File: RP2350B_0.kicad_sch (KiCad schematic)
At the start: 29 parts, among them CN4 W25Q128FVIQ_Connector, J6 Conn_01x02, X3 12MHz

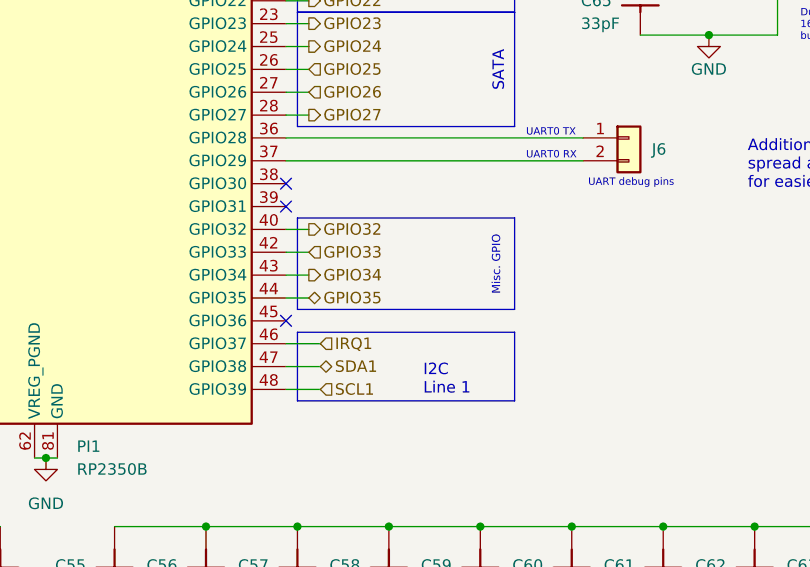
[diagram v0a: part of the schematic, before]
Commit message: Switched USB7206C IC to USB7205C
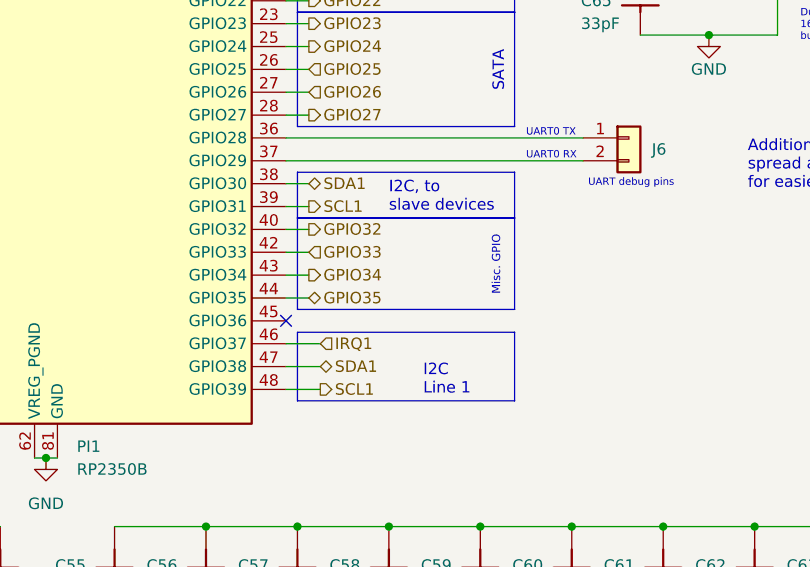
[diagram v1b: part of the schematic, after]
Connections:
- net SCL1: now also PI1.39 (GPIO31)
- net SDA1: now also PI1.38 (GPIO30)
- no-connect marks 8 -> 6
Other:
- note added: "I2C, to slave devices"
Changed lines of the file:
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@@
+		)
+	)
+	(rectangle
+		(start 129.54 111.76)
+		(end 153.67 116.84)
+		(stroke
+			(width 0)
+			(type default)
+		)
+		(fill
+			(type none)
 		)
 	)
@@
 		)
 	)
+	(text "I2C, to\nslave devices"
+		(exclude_from_sim no)
+		(at 139.7 114.554 0)
+		(effects
+			(font
+				(size 1.27 1.27)
+			)
+			(justify left)
+		)
+	)
 	(text "Dual 33pF capacitors is to achieve\n16.5pF + ~3pF (parasitic) = ~19.5pF total,\nbut 220ohm res is eyeballed, needs testing"
 		(exclude_from_sim no)
@@
 	)
 	(no_connect
-		(at 128.27 115.57)
-	)
-	(no_connect
-		(at 128.27 113.03)
-	)
-	(no_connect
 		(at 128.27 67.31)
 	)
@@
 	(wire
 		(pts
+			(xy 128.27 115.57) (xy 130.81 115.57)
+		)
+		(stroke
+			(width 0)
+			(type default)
+		)
+	)
+	(wire
+		(pts
 			(xy 130.81 80.01) (xy 128.27 80.01)
 		)
@@
 		(pts
 			(xy 130.81 102.87) (xy 128.27 102.87)
+		)
+		(stroke
+			(width 0)
+			(type default)
+		)
+	)
+	(wire
+		(pts
+			(xy 128.27 113.03) (xy 130.81 113.03)
 		)
 		(stroke
@@
 			)
 			(justify left bottom)
+		)
+	)
+	(hierarchical_label "SDA1"
+		(shape bidirectional)
+		(at 130.81 113.03 0)
+		(effects
+			(font
+				(size 1.27 1.27)
+			)
+			(justify left)
 		)
 	)
@@
 	)
 	(hierarchical_label "SCL1"
-		(shape input)
+		(shape output)
 		(at 132.08 135.89 0)
 		(effects
@@
 		(effects
 			(font
+				(size 1.27 1.27)
+			)
+			(justify left)
+		)
+	)
+	(hierarchical_label "SCL1"
+		(shape output)
+		(at 130.81 115.57 0)
+		(effects
+			(font

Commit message: Basic Function Review/Documentation of USB7205C
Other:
- note added: "Master I2C Channel 1"
- note added: "Slave I2C, to SG2002"
- note removed: "I2C Line 1"
- note removed: "I2C, to SG2002"
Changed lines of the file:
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@@
 		)
 	)
-	(text "I2C, to\nSG2002"
+	(text "Slave I2C,\nto SG2002"
 		(exclude_from_sim no)
-		(at 143.51 38.354 0)
+		(at 142.494 38.354 0)
 		(effects
 			(font
@@
 		)
 	)
-	(text "I2C\nLine 1"
+	(text "Master I2C\nChannel 1"
 		(exclude_from_sim no)
-		(at 143.51 134.874 0)
+		(at 142.24 134.62 0)
 		(effects
 			(font
